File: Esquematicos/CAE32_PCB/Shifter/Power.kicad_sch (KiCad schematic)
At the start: 19 parts, among them J6 USB_C_Receptacle_USB2.0, U3 AP2112K-3.3, U4 USBLC6-2P6

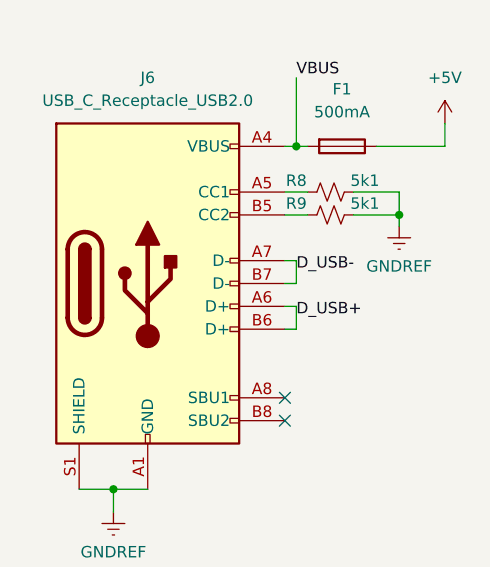
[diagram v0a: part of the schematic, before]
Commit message: update:Shifter PCB v1.1 Revision 1: Se cambia la posición de los "castelladed pins" a un solo lado, aumentando un poco el tamaño de la pcb pero reduciendo el costo de manufactura, ademas se añade la serigrafia correspondiente a la PCB
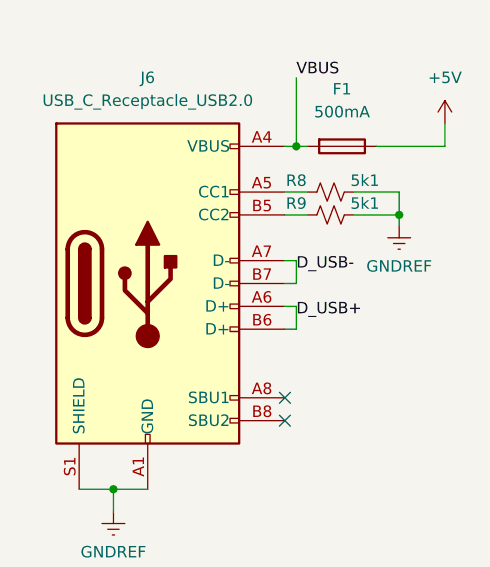
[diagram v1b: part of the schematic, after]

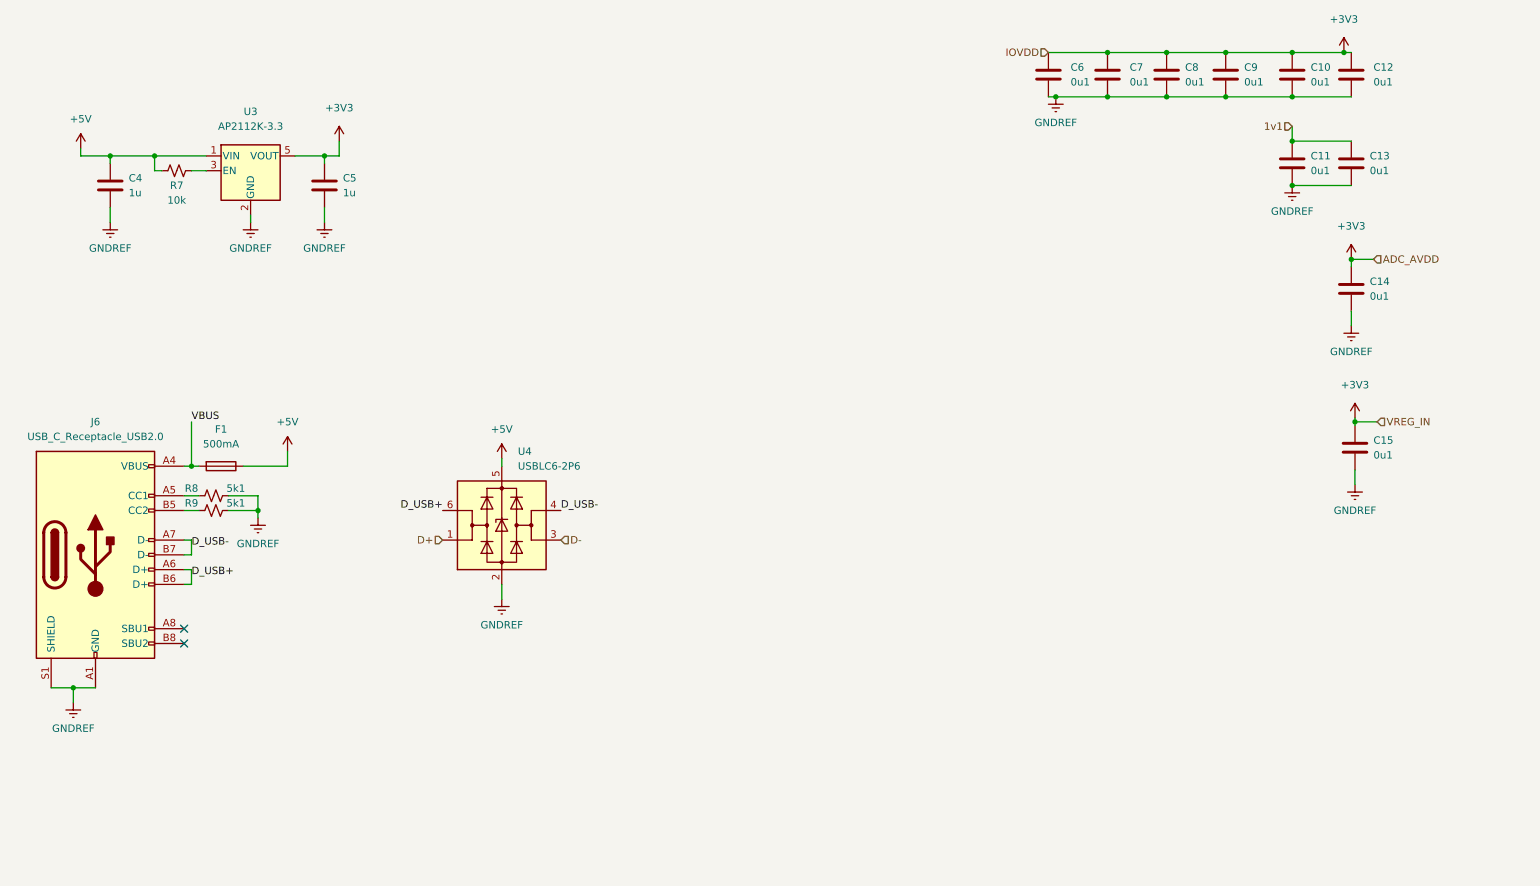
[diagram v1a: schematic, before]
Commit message: update: Se añade nombre y se separa a los diferentes componentes por categoria en el esquematico
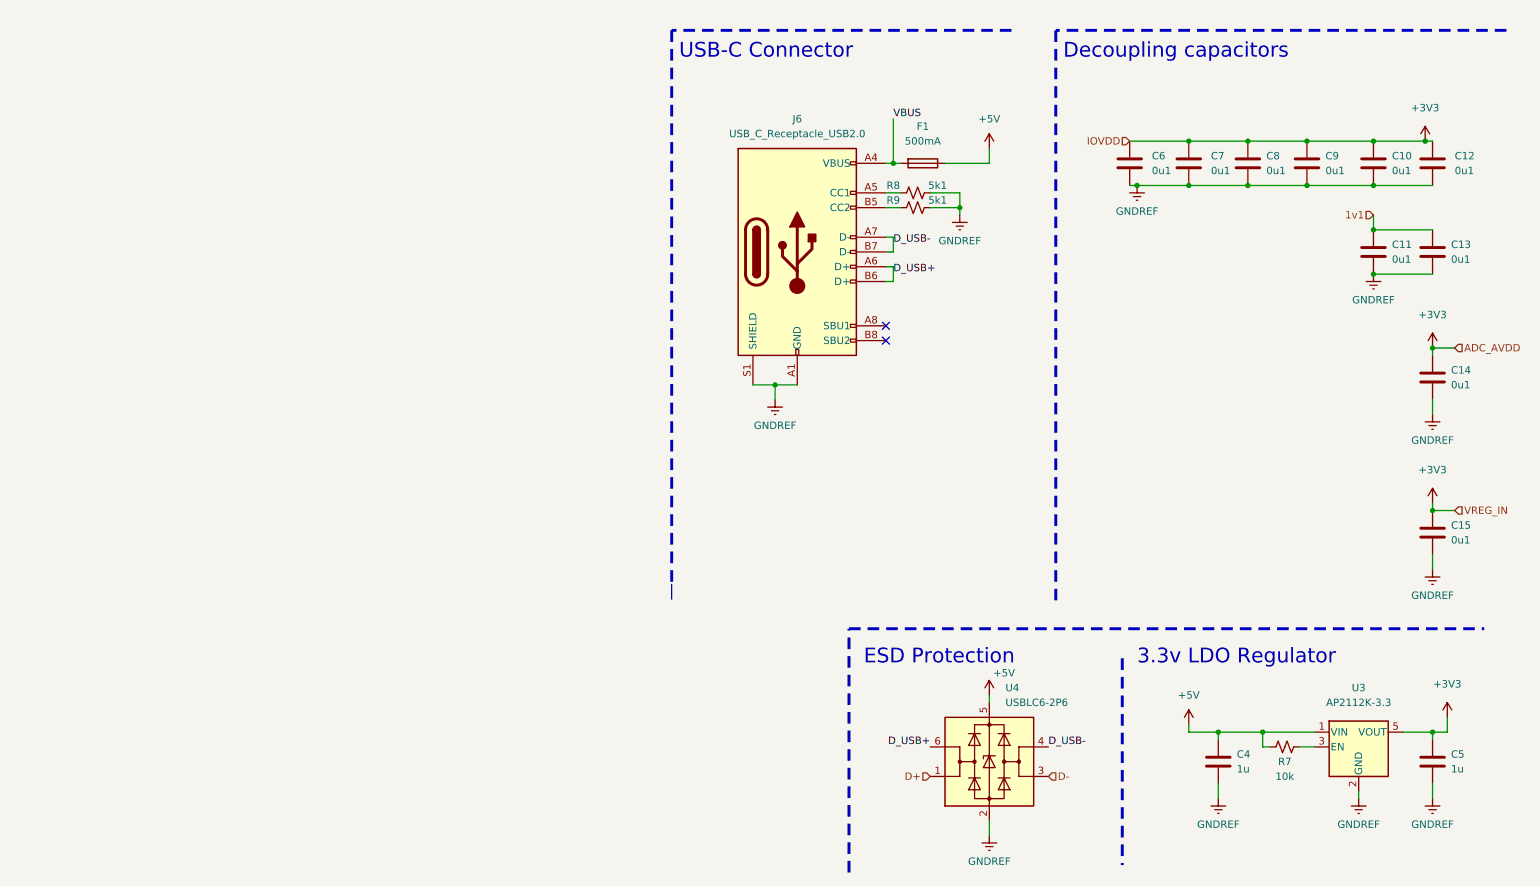
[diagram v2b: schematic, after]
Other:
- note added: "3.3v LDO Regulator"
- note added: "Decoupling capacitors"
- note added: "ESD Protection"
- note added: "USB-C Connector"
- title: (none) -> CAE32 Shifter
- moved on the sheet: C10, C11, C12, C13, C14, C15, C4, C5, C6, C7, C8, C9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

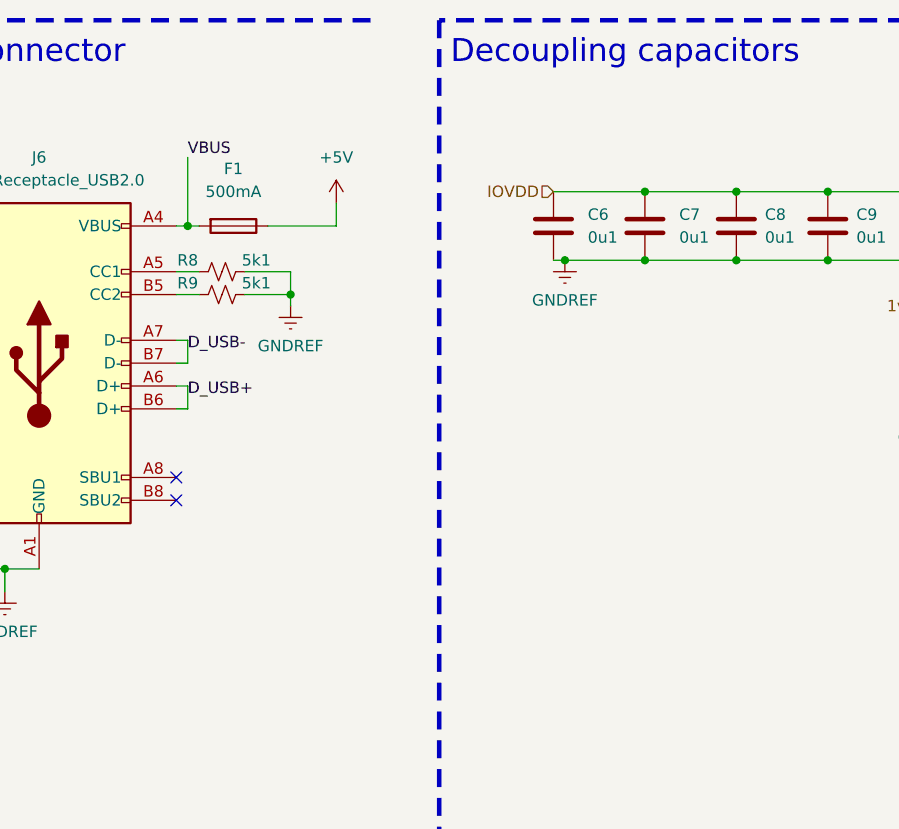
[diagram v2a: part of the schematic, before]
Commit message: update: changed the castelled holes for pin sockets and changed 0603 footprints to 0402
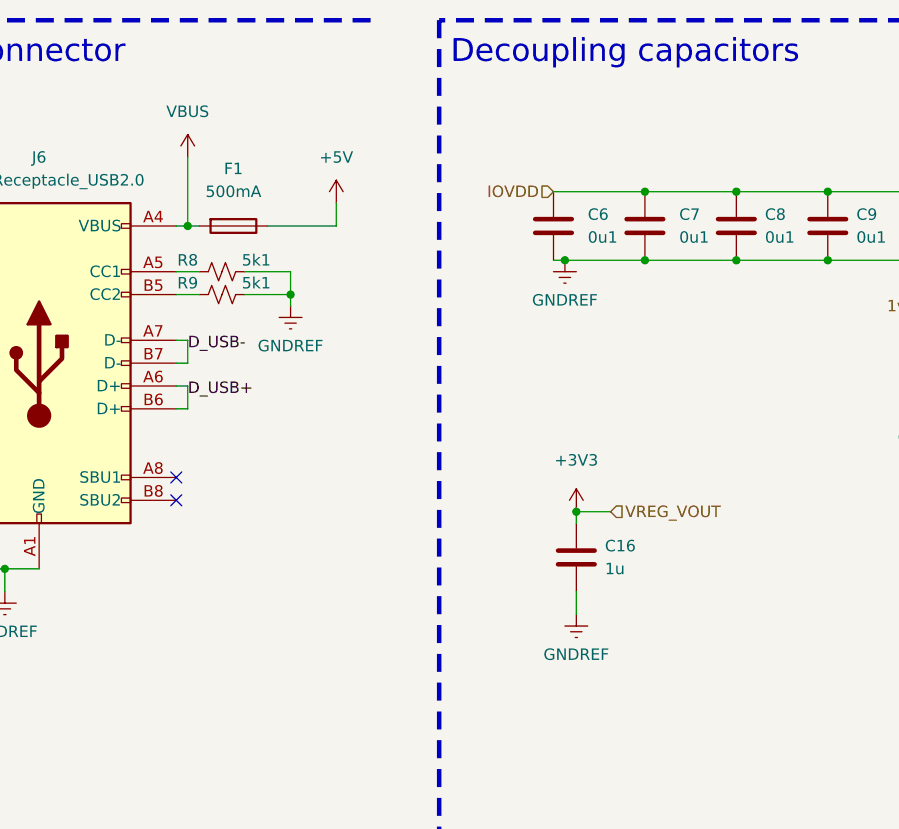
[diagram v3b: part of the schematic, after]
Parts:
- added C16: 1u, Capacitor_SMD:C_01005_0402Metric, symbol Device:C
- C10, C11, C12, C13, C14, C15, C4, C5, C6, C7, C8, C9: footprint Capacitor_SMD:C_0603_1608Metric_Pad1.08x0.95mm_HandSolder -> Capacitor_SMD:C_01005_0402Metric
- R7, R8, R9: footprint Resistor_SMD:R_0603_1608Metric_Pad0.98x0.95mm_HandSolder -> Resistor_SMD:R_0402_1005Metric
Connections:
- net +3V3: now also C16.1
- net GNDREF: now also C16.2

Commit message: chore: arrange of schematic elements
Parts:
- C10, C11, C12, C13, C14, C15, C6, C7, C8, C9: Vendor C42998 -> C913620
- C16: Vendor C42998 -> C141382
- C4, C5: Vendor C1592 -> C141382
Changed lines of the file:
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@@
       (effects (font (size 1.27 1.27)) hide)
     )
-    (property "Vendor" "C42998" (at 269.24 81.28 0)
+    (property "Vendor" "C913620" (at 269.24 81.28 0)
       (effects (font (size 1.27 1.27)) hide)
     )
@@
       (effects (font (size 1.27 1.27)) hide)
     )
-    (property "Vendor" "C42998" (at 219.71 81.28 0)
+    (property "Vendor" "C141382" (at 219.71 81.28 0)
       (effects (font (size 1.27 1.27)) hide)
     )
@@
       (effects (font (size 1.27 1.27)) hide)
     )
-    (property "Vendor" "C42998" (at 269.24 59.69 0)
+    (property "Vendor" "C913620" (at 269.24 59.69 0)
       (effects (font (size 1.27 1.27)) hide)
     )
@@
       (effects (font (size 1.27 1.27)) hide)
     )
-    (property "Vendor" "C1592" (at 232.41 147.32 0)
+    (property "Vendor" "C141382" (at 232.41 147.32 0)
       (effects (font (size 1.27 1.27)) hide)
     )
@@
       (effects (font (size 1.27 1.27)) hide)
     )
-    (property "Vendor" "C42998" (at 247.65 44.45 0)
+    (property "Vendor" "C913620" (at 247.65 44.45 0)
       (effects (font (size 1.27 1.27)) hide)
     )
@@
       (effects (font (size 1.27 1.27)) hide)
     )
-    (property "Vendor" "C42998" (at 237.49 44.45 0)
+    (property "Vendor" "C913620" (at 237.49 44.45 0)
       (effects (font (size 1.27 1.27)) hide)
     )
@@
       (effects (font (size 1.27 1.27)) hide)
     )
-    (property "Vendor" "C42998" (at 227.33 44.45 0)
+    (property "Vendor" "C913620" (at 227.33 44.45 0)
       (effects (font (size 1.27 1.27)) hide)
     )
@@
       (effects (font (size 1.27 1.27)) hide)
     )
-    (property "Vendor" "C42998" (at 259.08 44.45 0)
+    (property "Vendor" "C913620" (at 259.08 44.45 0)
       (effects (font (size 1.27 1.27)) hide)
     )
@@
       (effects (font (size 1.27 1.27)) hide)
     )
-    (property "Vendor" "C42998" (at 217.17 44.45 0)
+    (property "Vendor" "C913620" (at 217.17 44.45 0)
       (effects (font (size 1.27 1.27)) hide)
     )
@@
       (effects (font (size 1.27 1.27)) hide)
     )
-    (property "Vendor" "C1592" (at 269.24 147.32 0)
+    (property "Vendor" "C141382" (at 269.24 147.32 0)
       (effects (font (size 1.27 1.27)) hide)
     )
@@
       (effects (font (size 1.27 1.27)) hide)
     )
-    (property "Vendor" "C42998" (at 269.24 107.95 0)
+    (property "Vendor" "C913620" (at 269.24 107.95 0)
       (effects (font (size 1.27 1.27)) hide)
     )
@@
       (effects (font (size 1.27 1.27)) hide)
     )
-    (property "Vendor" "C42998" (at 269.24 44.45 0)
+    (property "Vendor" "C913620" (at 269.24 44.45 0)
       (effects (font (size 1.27 1.27)) hide)
     )
@@
       (effects (font (size 1.27 1.27)) hide)
     )
-    (property "Vendor" "C42998" (at 259.08 59.69 0)
-      (effects (font (size 1.27 1.27)) hide)
-    )
+    (property "Vendor" "C913620" (at 259.08 59.69 0)
+      (effects (font (size 1.27 1.27)) hide)
+    )
